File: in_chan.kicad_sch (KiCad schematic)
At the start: 8 parts, among them U7 MAX31910AUI+

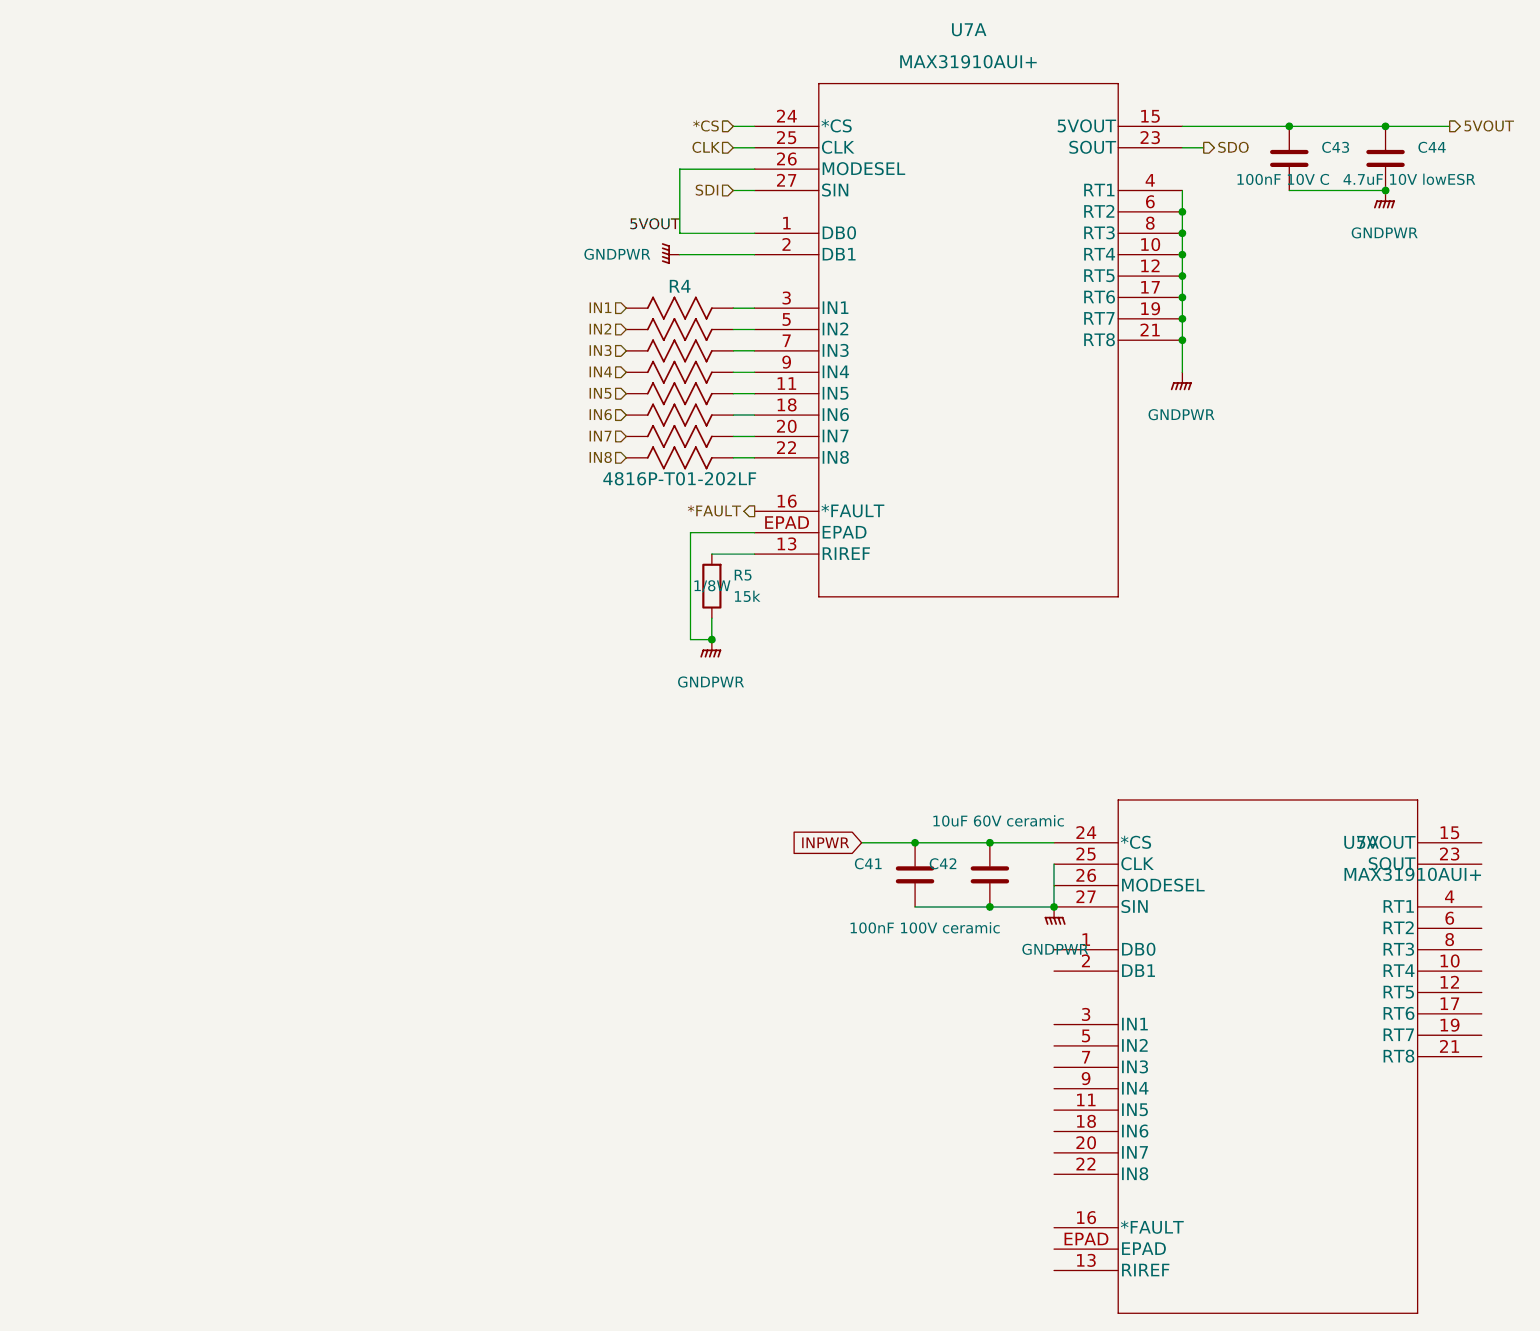
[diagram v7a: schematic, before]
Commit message: fix a few warnings
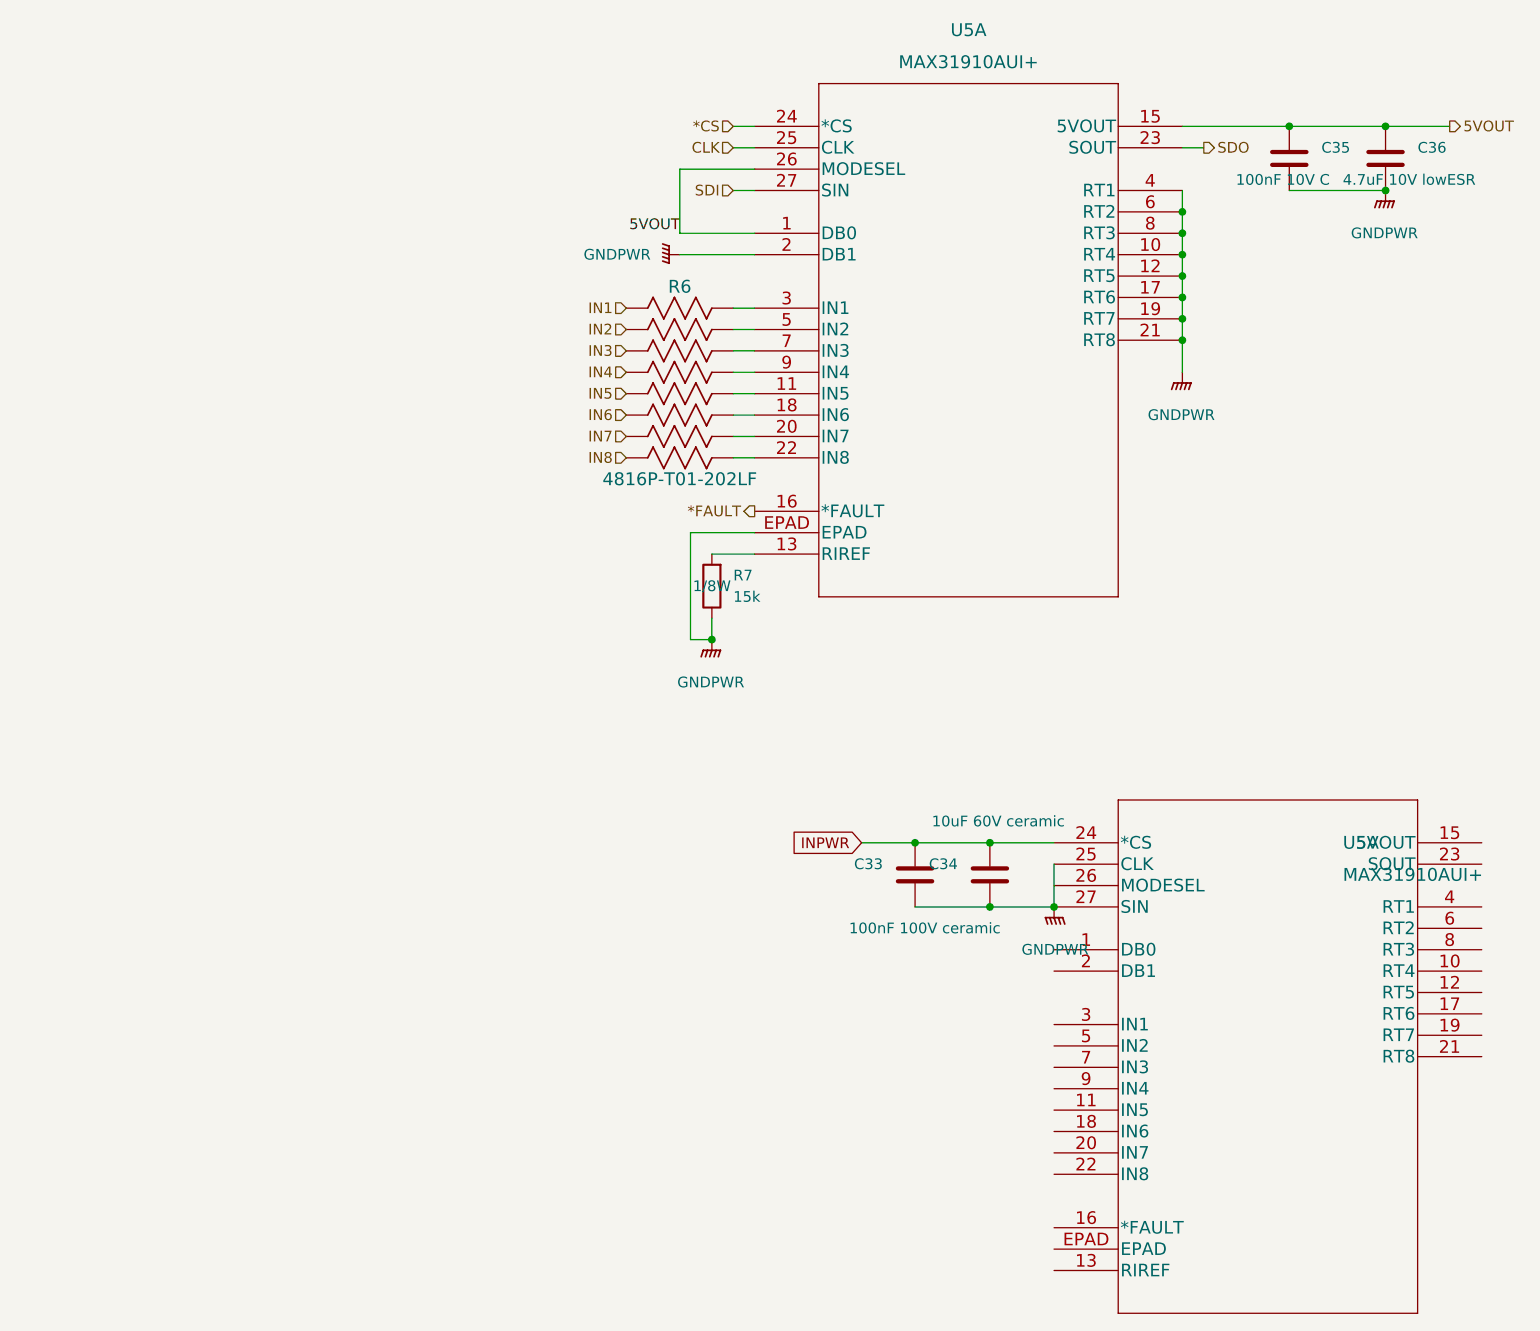
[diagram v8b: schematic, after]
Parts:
- renumbered C41 to C33, C42 to C34, C43 to C35, C44 to C36, R4 to R6, R5 to R7, U7 to U5
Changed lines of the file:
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@@
   (symbol (lib_id "power:GNDPWR") (at 163.83 119.38 0)
     (in_bom yes) (on_board yes) (fields_autoplaced)
-    (property "Reference" "#PWR051" (id 0) (at 163.83 124.46 0)
+    (property "Reference" "#PWR031" (id 0) (at 163.83 124.46 0)
       (effects (font (size 1.27 1.27)) hide)
     )
@@
   (symbol (lib_id "Device:R") (at 163.83 113.03 180)
     (in_bom yes) (on_board yes)
-    (property "Reference" "R5" (id 0) (at 166.37 111.76 0)
+    (property "Reference" "R7" (id 0) (at 166.37 111.76 0)
       (effects (font (size 1.27 1.27)) (justify right))
     )
@@
   (symbol (lib_id "power:GNDPWR") (at 204.47 151.13 0) (mirror y)
     (in_bom yes) (on_board yes) (fields_autoplaced)
-    (property "Reference" "#PWR052" (id 0) (at 204.47 156.21 0)
+    (property "Reference" "#PWR032" (id 0) (at 204.47 156.21 0)
       (effects (font (size 1.27 1.27)) hide)
     )
@@
   (symbol (lib_id "power:GNDPWR") (at 243.84 66.04 0)
     (in_bom yes) (on_board yes) (fields_autoplaced)
-    (property "Reference" "#PWR054" (id 0) (at 243.84 71.12 0)
+    (property "Reference" "#PWR034" (id 0) (at 243.84 71.12 0)
       (effects (font (size 1.27 1.27)) hide)
     )
@@
   (symbol (lib_id "Device:C") (at 243.84 62.23 0)
     (in_bom yes) (on_board yes)
-    (property "Reference" "C44" (id 0) (at 247.65 60.9599 0)
+    (property "Reference" "C36" (id 0) (at 247.65 60.9599 0)
       (effects (font (size 1.27 1.27)) (justify left))
     )
@@
   (symbol (lib_id "Maxim industrial IO:MAX31910AUI+") (at 204.47 143.51 0)
     (in_bom yes) (on_board yes) (fields_autoplaced)
-    (property "Reference" "U7" (id 0) (at 238.76 143.51 0)
+    (property "Reference" "U5" (id 0) (at 238.76 143.51 0)
       (effects (font (size 1.524 1.524)) (justify left))
     )
@@
   (symbol (lib_id "Device:C") (at 187.96 147.32 0) (mirror y)
     (in_bom yes) (on_board yes)
-    (property "Reference" "C41" (id 0) (at 184.15 146.0499 0)
+    (property "Reference" "C33" (id 0) (at 184.15 146.0499 0)
       (effects (font (size 1.27 1.27)) (justify left))
     )
@@
   (symbol (lib_id "power:GNDPWR") (at 219.71 87.63 0)
     (in_bom yes) (on_board yes) (fields_autoplaced)
-    (property "Reference" "#PWR053" (id 0) (at 219.71 92.71 0)
+    (property "Reference" "#PWR033" (id 0) (at 219.71 92.71 0)
       (effects (font (size 1.27 1.27)) hide)
     )
@@
   (symbol (lib_id "Device:C") (at 232.41 62.23 0)
     (in_bom yes) (on_board yes)
-    (property "Reference" "C43" (id 0) (at 236.22 60.9599 0)
+    (property "Reference" "C35" (id 0) (at 236.22 60.9599 0)
       (effects (font (size 1.27 1.27)) (justify left))
     )
@@
   (symbol (lib_id "power:GNDPWR") (at 160.02 73.66 270)
     (in_bom yes) (on_board yes)
-    (property "Reference" "#PWR050" (id 0) (at 154.94 73.66 0)
+    (property "Reference" "#PWR030" (id 0) (at 154.94 73.66 0)
       (effects (font (size 1.27 1.27)) hide)
     )
@@
   (symbol (lib_id "Device:C") (at 196.85 147.32 0) (mirror y)
     (in_bom yes) (on_board yes)
-    (property "Reference" "C42" (id 0) (at 193.04 146.0499 0)
+    (property "Reference" "C34" (id 0) (at 193.04 146.0499 0)
       (effects (font (size 1.27 1.27)) (justify left))
     )
@@
   (symbol (lib_id "Num-IO:4816P-T01-103LF") (at 153.67 80.01 0)
     (in_bom yes) (on_board yes)
-    (property "Reference" "R4" (id 0) (at 160.02 77.47 0)
+    (property "Reference" "R6" (id 0) (at 160.02 77.47 0)
       (effects (font (size 1.524 1.524)))
     )
@@
   (symbol (lib_id "Maxim industrial IO:MAX31910AUI+") (at 168.91 58.42 0)
     (in_bom yes) (on_board yes) (fields_autoplaced)
-    (property "Reference" "U7" (id 0) (at 194.31 46.99 0)
-      (effects (font (size 1.524 1.524)))
-    )
+    (property "Reference" "U5" (id 0) (at 194.31 46.99 0)
+      (effects (font (size 1.524 1.524)))
+    )
